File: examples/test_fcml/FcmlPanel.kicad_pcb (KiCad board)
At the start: 2 copper layers, 109 x 72 mm, 243 parts, among them J1 COM-15111 (Sparkfun), J2 COM-15111 (Sparkfun), J3 B2B-PH-K (JST), J4 B2B-PH-K (JST), J5 PinHeader1.27 Shrouded 2x5 (G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, J6 PinHeader1.27 Shrouded 2x5 (G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, Q1 HSM4410 (HUASHUO) - 30V 12A 2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, Q2 HSM4410 (HUASHUO) - 30V 12A 2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, Q3 HSM4410 (HUASHUO) - 30V 12A 2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, Q4 HSM4410 (HUASHUO) - 30V 12A 2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, Q5 HSM4410 (HUASHUO) - 30V 12A 2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, Q6 HSM4410 (HUASHUO) - 30V 12A 2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, SW1 5.1mm switch, SW2 5.1mm switch, U1 LD1117S33TR (STMicroelectroni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, U10 ICE40UP5K-SG48 (Lattice Semic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, U11 LD1117S12TR (STMicroelectroni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, U12 W25Q128JVSIQ (Winbond Electro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, U13 PGB102ST23 (Littelfuse), U14 RP2040 (Raspberry Pi), U15 W25Q128JVSIQ (Winbond Electro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, U16 PGB102ST23 (Littelfuse), U17 Duck, U18 Lemur, U19 IdDots4, U2 AP3012K (Diodes Incorporated), U3 IR2301 (Infineon Technologies), U4 AP2204K-3.3 (Diodes Incorpora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, U5 CBMuD1200L (Corebai), U6 IR2301 (Infineon Technologies), U7 AP2204K-3.3 (Diodes Incorpora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, U8 CBMuD1200L (Corebai), U9 IR2301 (Infineon Technologies)

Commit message: update
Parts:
- added UC4: , Capacitor_SMD:C_0603_1608Metric, F.Cu at (132.0, 156.0)
- added UC5: , Capacitor_SMD:C_1206_3216Metric, F.Cu at (132.0, 163.0)
- added UU6: IdDots4, edg:Indicator_IdDots_4, B.Cu at (107.0, 159.0)
- UU3: value Duck -> AP2204K-3.3 (Diodes Incorporated); footprint edg:Symbol_Duckling -> Package_TO_SOT_SMD:SOT-23-5; moved to F.Cu
- UU4: value Lemur -> Duck; footprint edg:Symbol_LemurSmall -> edg:Symbol_Duckling
- UU5: value IdDots4 -> Lemur; footprint edg:Indicator_IdDots_4 -> edg:Symbol_LemurSmall
- moved UJ2 31.6 mm to (138.7, 155.2), turned to 0 degrees
- moved UH1 27.9 mm to (136.7, 164.0), turned to 0 degrees
- moved UH3 27.9 mm to (136.7, 154.0), turned to 0 degrees
- moved UJ1 21.0 mm to (110.0, 159.0), turned to -90 degrees
- moved UU5 18.0 mm to (116.0, 159.0), turned to 180 degrees
- moved UC1 16.4 mm to (127.0, 164.0), turned to 180 degrees
- moved UD2 16.4 mm to (127.0, 154.0), turned to 0 degrees
- moved UH2 14.9 mm to (115.0, 164.0), turned to 0 degrees
- moved UU4 14.0 mm to (111.0, 159.0), turned to 180 degrees
- moved UC2 11.2 mm to (118.0, 164.0), turned to 180 degrees
- moved UC3 11.2 mm to (123.0, 164.0), turned to 0 degrees
- moved UD1 11.2 mm to (118.0, 154.0), turned to 0 degrees
- moved UR3 11.2 mm to (123.0, 154.0), turned to 180 degrees
- moved UU1 9.00 mm to (125.0, 159.0), turned to 0 degrees
- moved UR1 7.81 mm to (118.0, 156.0), turned to 180 degrees
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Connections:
- UJ2 pad 4: vusb -> v3v3
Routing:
- net (no net): track 453.9 -> 466.9 mm
- net v3v3: track 367.2 -> 378.7 mm
- net vusb: track 237.1 -> 247.1 mm, vias 17 -> 19
- net gnd: track 149.6 -> 152.5 mm, vias 110 -> 113
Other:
- board size 109 x 72 mm -> 115 x 72 mm
- board text added: "3v3"
- board text removed: "+5v"

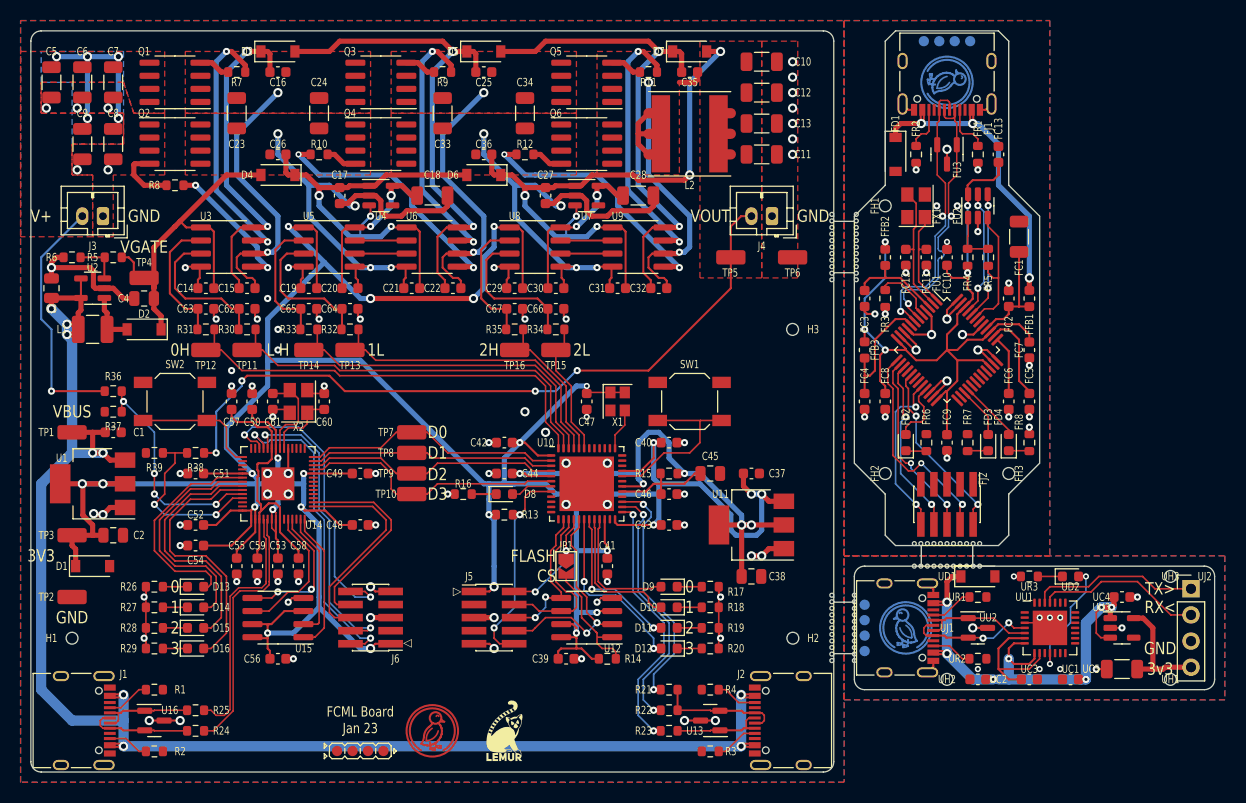
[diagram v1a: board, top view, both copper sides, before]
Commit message: fix so-8 w25q
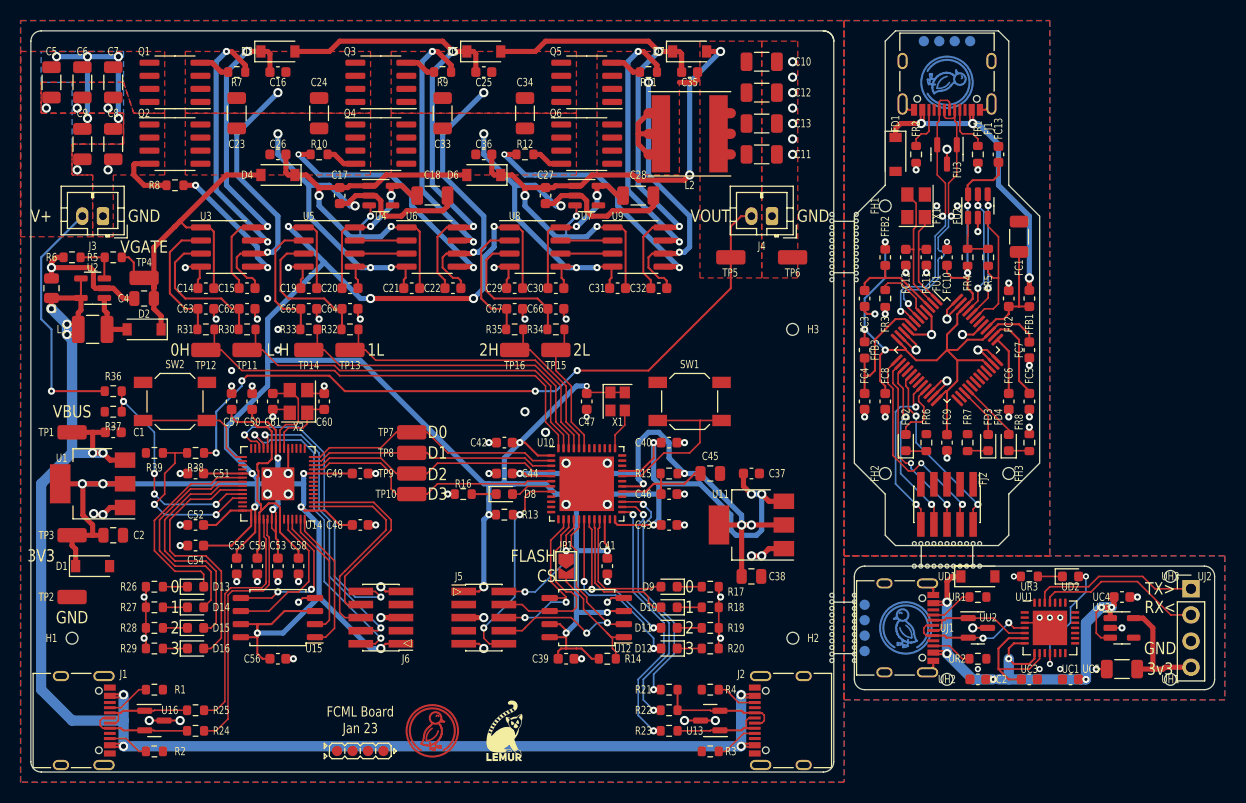
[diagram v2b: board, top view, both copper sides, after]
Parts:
- U12, U15: footprint Package_SO:SOIC-8_3.9x4.9mm_P1.27mm -> Package_SO:SOIC-8_5.23x5.23mm_P1.27mm
- moved J5 1.00 mm to (70.0, 158.0)
- moved J6 1.00 mm to (60.0, 158.0)
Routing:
- net v3v3: track 378.7 -> 387.7 mm
- net fpga.ic.spi_config.mosi: track 14.6 -> 17.5 mm
- net fpga.ic.spi_config.miso: track 22.5 -> 25.1 mm
- net mcu.gpio.led_0: track 21.3 -> 20.2 mm
- net mcu.ic.qspi.sck: track 13.6 -> 14.7 mm
- net mcu.ic.qspi.mosi: track 13.9 -> 15.0 mm
- net mcu.swd.swd.reset: track 30.3 -> 31.3 mm
- net fpga.ic.spi_config_cs: track 11.4 -> 12.4 mm
- net fpga.ic.spi_config.sck: track 16.7 -> 17.7 mm
- net mcu.gpio.led_1: track 23.1 -> 22.2 mm
- net mcu.usb_chain_0.d_N: track 24.3 -> 23.6 mm
- net mcu.usb_chain_0.d_P: track 25.1 -> 25.7 mm
